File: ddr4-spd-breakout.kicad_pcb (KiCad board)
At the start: 4 copper layers, 152.9 x 45 mm, 66 parts, among them IC1 MIC5317-2.5YM5-TR, J1 WE_629105150521, J4 0022232041, U1 FT2232HL-REEL, U14 2199155-1, U2 NCP163ASN330T1G, U8 PCA9517ADMR2G, Y1 KX-7_12,MHz

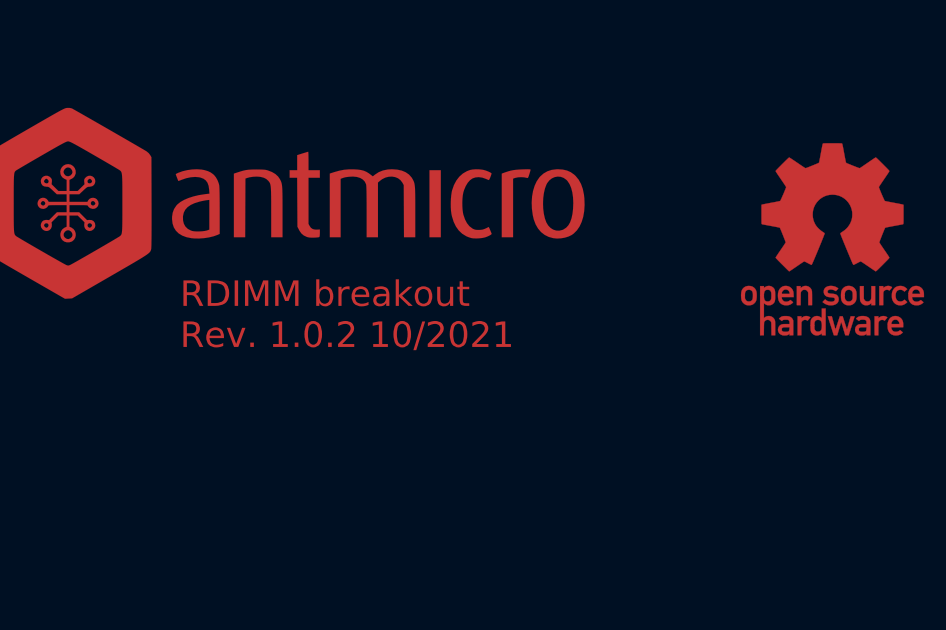
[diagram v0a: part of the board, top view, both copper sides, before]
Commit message: Update naming convention
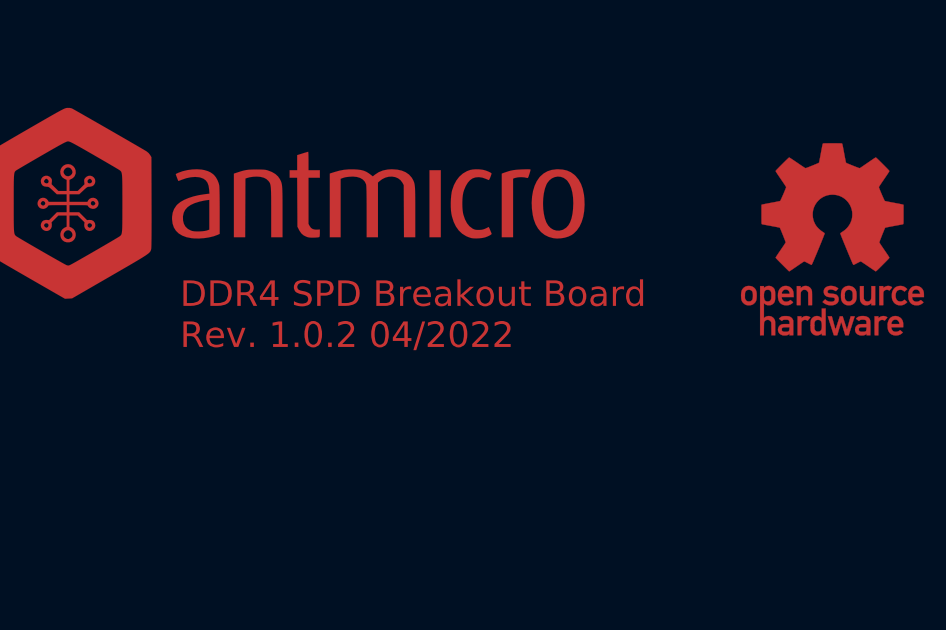
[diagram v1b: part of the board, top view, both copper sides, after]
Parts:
- 1V8_FT1, 2V5, 3V3, 5V0, TP1, TP12, TP2: footprint rdimm-breakout-footprints:Testpoint_smd_1mm -> ddr4-spd-breakout-footprints:Testpoint_smd_1mm
- C1, C10, C11, C12, C13, C14, C15, C16, C17, C18, C19, C2, C20, C21, C22, C23, C3, C4, C5, C6, C7, C8, C9: footprint rdimm-breakout-footprints:0402-cap -> ddr4-spd-breakout-footprints:0402-cap
- D1: footprint rdimm-breakout-footprints:TPD2E009DRTR -> ddr4-spd-breakout-footprints:TPD2E009DRTR
- FB1, FB2, FB3: footprint rdimm-breakout-footprints:0603 -> ddr4-spd-breakout-footprints:0603
- IC1, U2: footprint rdimm-breakout-footprints:SOT-23-5 -> ddr4-spd-breakout-footprints:SOT-23-5
- J1: footprint rdimm-breakout-footprints:USB_Micro_B_Female_629105150521 -> ddr4-spd-breakout-footprints:USB_Micro_B_Female_629105150521
- J4: footprint rdimm-breakout-footprints:PinHeader_1x4_P2.54mm_Drill1.02mm -> ddr4-spd-breakout-footprints:PinHeader_1x4_P2.54mm_Drill1.02mm
- N1: footprint rdimm-breakout-footprints:oshw-logo -> ddr4-spd-breakout-footprints:oshw-logo
- N2: footprint rdimm-breakout-footprints:antmicro-logo_scaled_20mm -> ddr4-spd-breakout-footprints:antmicro-logo_scaled_20mm
- PWR1: footprint rdimm-breakout-footprints:LED_0603 -> ddr4-spd-breakout-footprints:LED_0603
- R1, R12, R5, R6: footprint rdimm-breakout-footprints:0603-res -> ddr4-spd-breakout-footprints:0603-res
- R10, R11, R119, R164, R165, R166, R167, R168, R169, R170, R2, R3, R4, R7, R8, R9: footprint rdimm-breakout-footprints:0402-res -> ddr4-spd-breakout-footprints:0402-res
- S3: footprint rdimm-breakout-footprints:Switch_Slide_MSS3 -> ddr4-spd-breakout-footprints:Switch_Slide_MSS3
- U1: footprint rdimm-breakout-footprints:LQFP-64_10x10mm -> ddr4-spd-breakout-footprints:LQFP-64_10x10mm
- U14: footprint rdimm-breakout-footprints:2199155-1 -> ddr4-spd-breakout-footprints:2199155-1
- U8: footprint rdimm-breakout-footprints:TSSOP-8_W3mm -> ddr4-spd-breakout-footprints:TSSOP-8_W3mm
- Y1: footprint rdimm-breakout-footprints:KX-7 -> ddr4-spd-breakout-footprints:KX-7
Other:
- board text added: "DDR4 SPD Breakout Board Rev. 1.0.2 04/2022"
- board text removed: "RDIMM breakout Rev. 1.0.2 10/2021"
